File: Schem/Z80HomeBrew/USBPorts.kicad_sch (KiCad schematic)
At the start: 26 parts, among them J4 USB_A, J5 USB_A, U15 MAX3421EETJ_T, U16 FE1.1S-BSOP28BCN, U17 4050, Y2 ABL-12.000MHZ-B2, Y3 ABL-12.000MHZ-B2

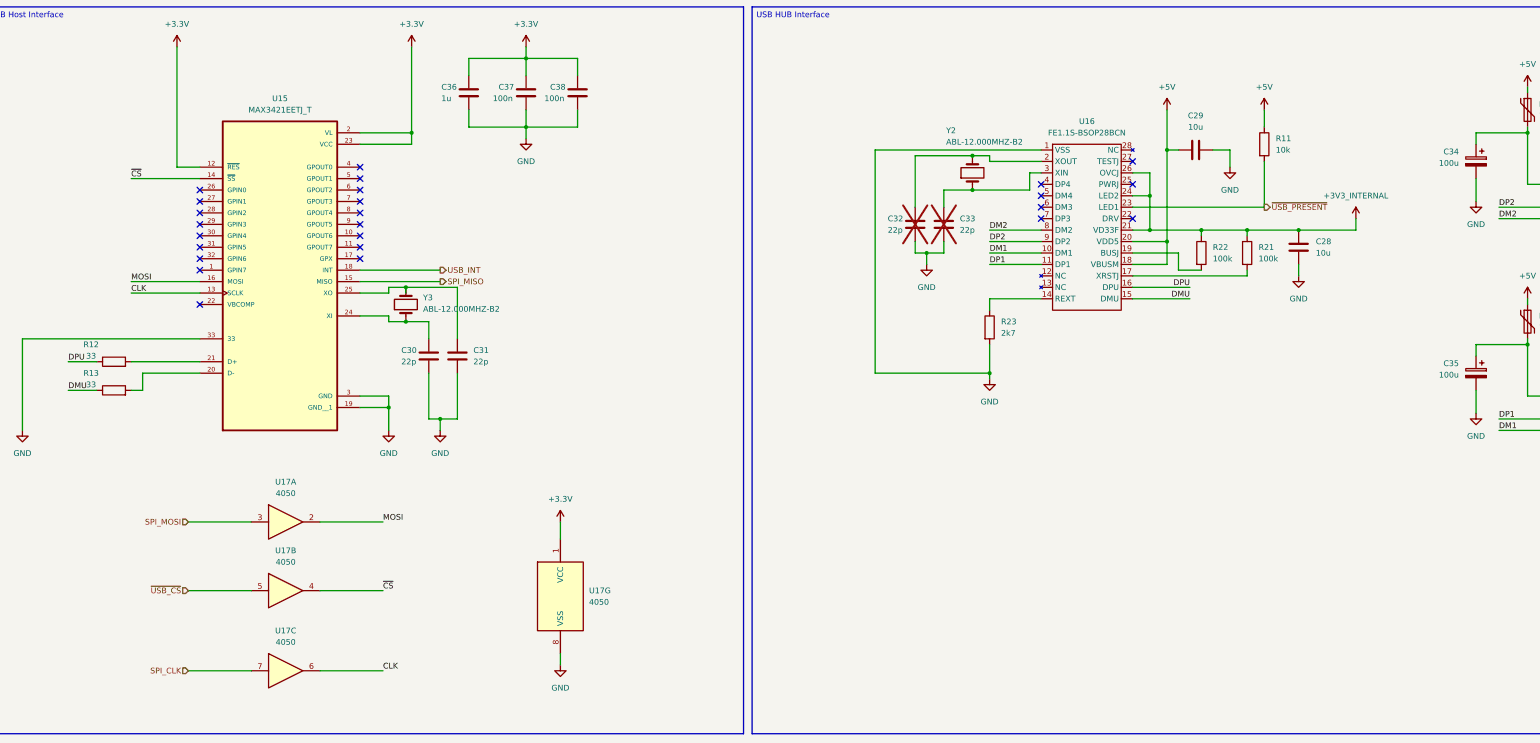
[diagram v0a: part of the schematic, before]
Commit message: Video block added. fixed some issues with parts...
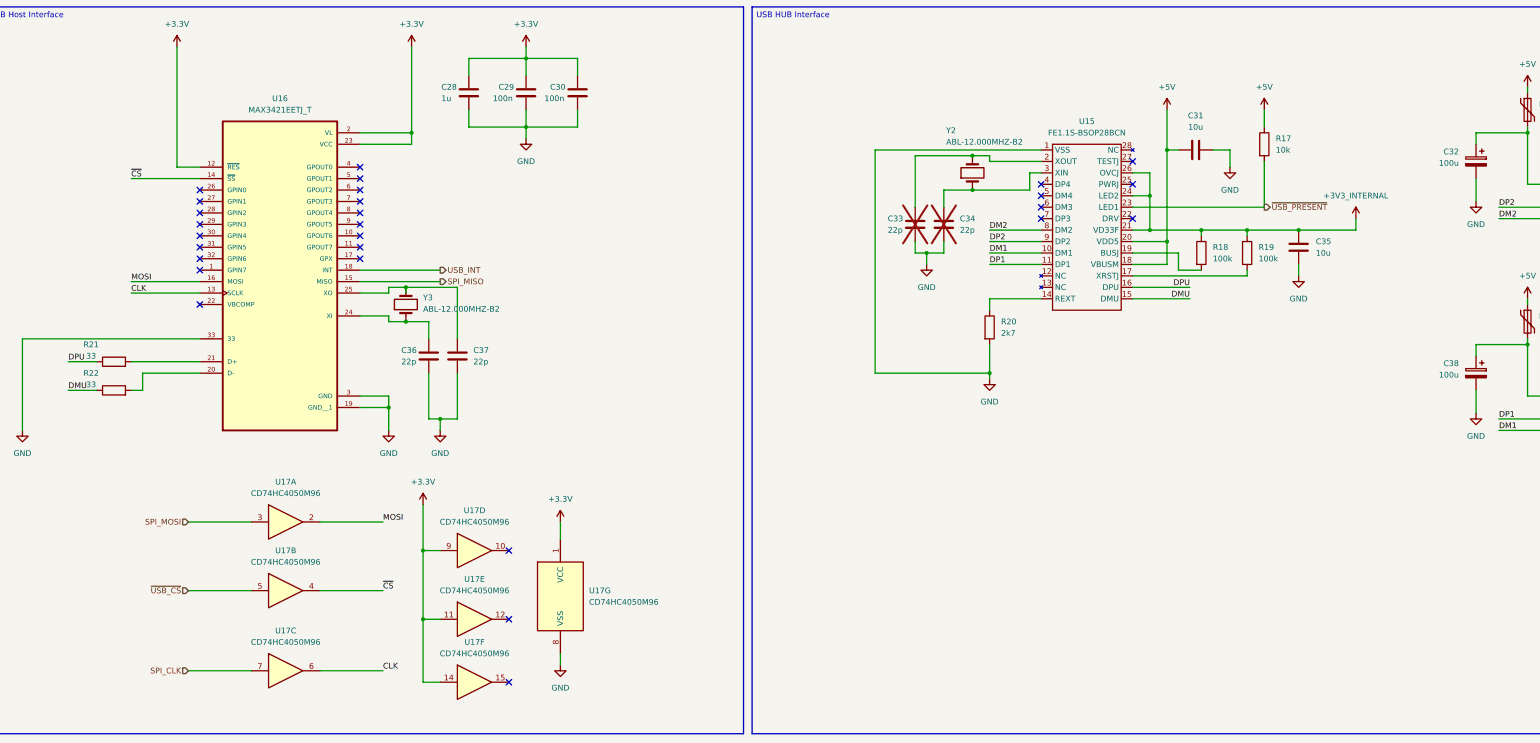
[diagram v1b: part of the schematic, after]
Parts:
- added unit 5 of U17
- added unit 4 of U17
- added unit 6 of U17
- C32: renamed from C34; footprint (none) -> Capacitor_SMD:C_0603_1608Metric
- C38: renamed from C35; footprint (none) -> Capacitor_SMD:C_0603_1608Metric
- U17: value 4050 -> CD74HC4050M96; footprint (none) -> Footprints:SOIC127P600X175-16N
- renumbered C36 to C28, C37 to C29, C38 to C30, C29 to C31, C32 to C33, C33 to C34, C28 to C35, C30 to C36, C31 to C37, R11 to R17, R22 to R18, R21 to R19, R23 to R20, R12 to R21, R13 to R22, U16 to U15, U15 to U16
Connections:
- net +3.3V: now also U17.11, U17.14, U17.9
- no-connect marks 25 -> 28

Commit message: Completed schematics
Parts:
- added R37: 0, NetTie:NetTie-2_SMD_Pad0.5mm, symbol Device:R
- J4, J5: value USB_A -> 0480370001; footprint (none) -> Footprints:CONN_480370001_MOL
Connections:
- net +3V3_INTERNAL: no longer U15.24 (LED2)
- net GND: now also R37.1; no longer U16.33
- new net: R37.2, U16.33
- no-connect marks 28 -> 29
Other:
- moved on the sheet: Y3

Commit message: Finally found a name "Zephyr-80" for the brew and committing the first pbc
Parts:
- added J14, J15: Conn_01x04, Connector_PinSocket_2.54mm:PinSocket_1x04_P2.54mm_Vertical, symbol Connector_Generic:Conn_01x04
- R37: now not fitted
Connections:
- net +3.3V: no longer U17.11, U17.14, U17.9
- net DM1: now also J15.2 (Pin_2)
- net DM2: now also J14.2 (Pin_2)
- net DP1: now also J15.4 (Pin_4)
- net DP2: now also J14.4 (Pin_4)
- net GND: now also U17.11, U17.14, U17.9, J14.3 (Pin_3), J15.3 (Pin_3)
- net at C36.2, U16.24 (XI): now also Y3.2; no longer Y3.1
- net at C37.2, U16.25 (XO): now also Y3.1; no longer Y3.2
- net VBUS_PIN2: now reaches C32.1, F2.2, J4.1 (VBUS)
- net VBUS_PIN2: now also J14.1 (Pin_1)
- net at C34.2, U15.3 (XIN): now also Y2.2; no longer Y2.1
- net at C33.2, U15.2 (XOUT): now also Y2.1; no longer Y2.2
- net VBUS_PIN1: now reaches C38.1, F3.2, J5.1 (VBUS)
- net VBUS_PIN1: now also J15.1 (Pin_1)
- net DMU renamed D-
- net DPU renamed D+
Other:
- note added: "Alternative header for USB Port"

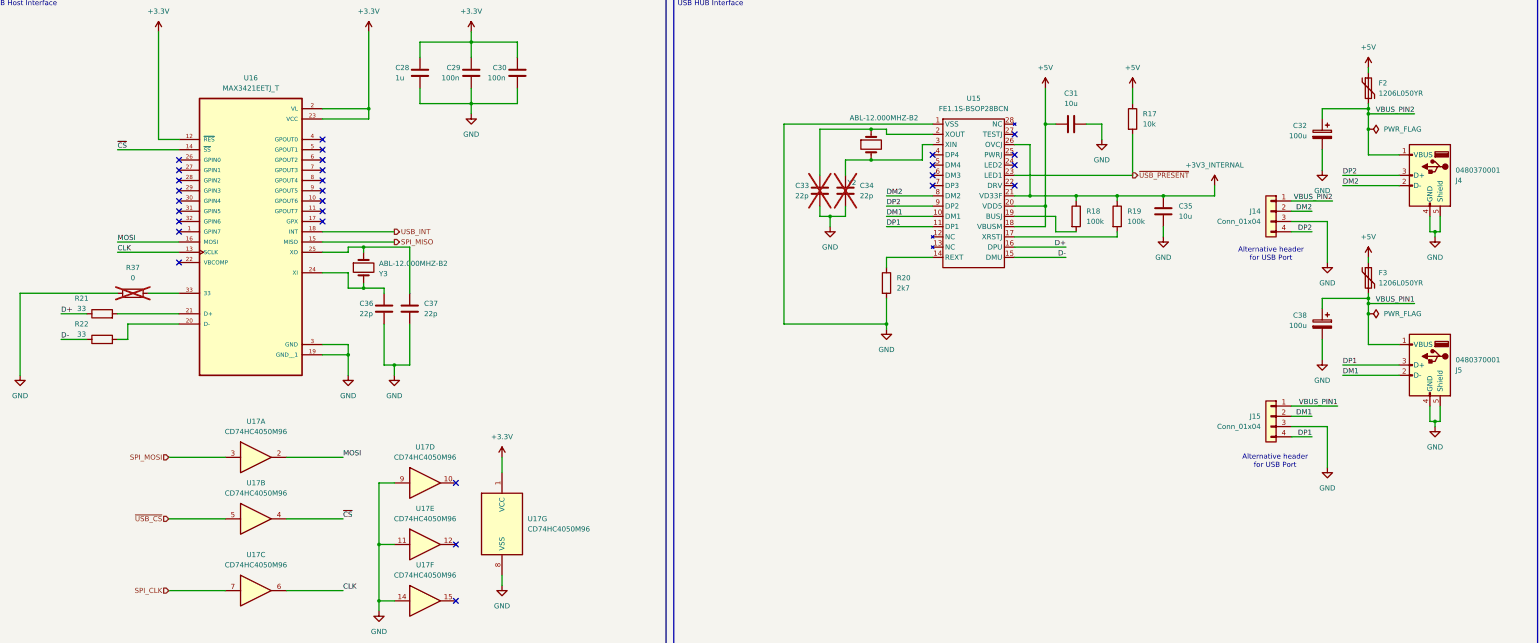
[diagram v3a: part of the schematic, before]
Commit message: Added pBITzBackplane and MezzanineConnector
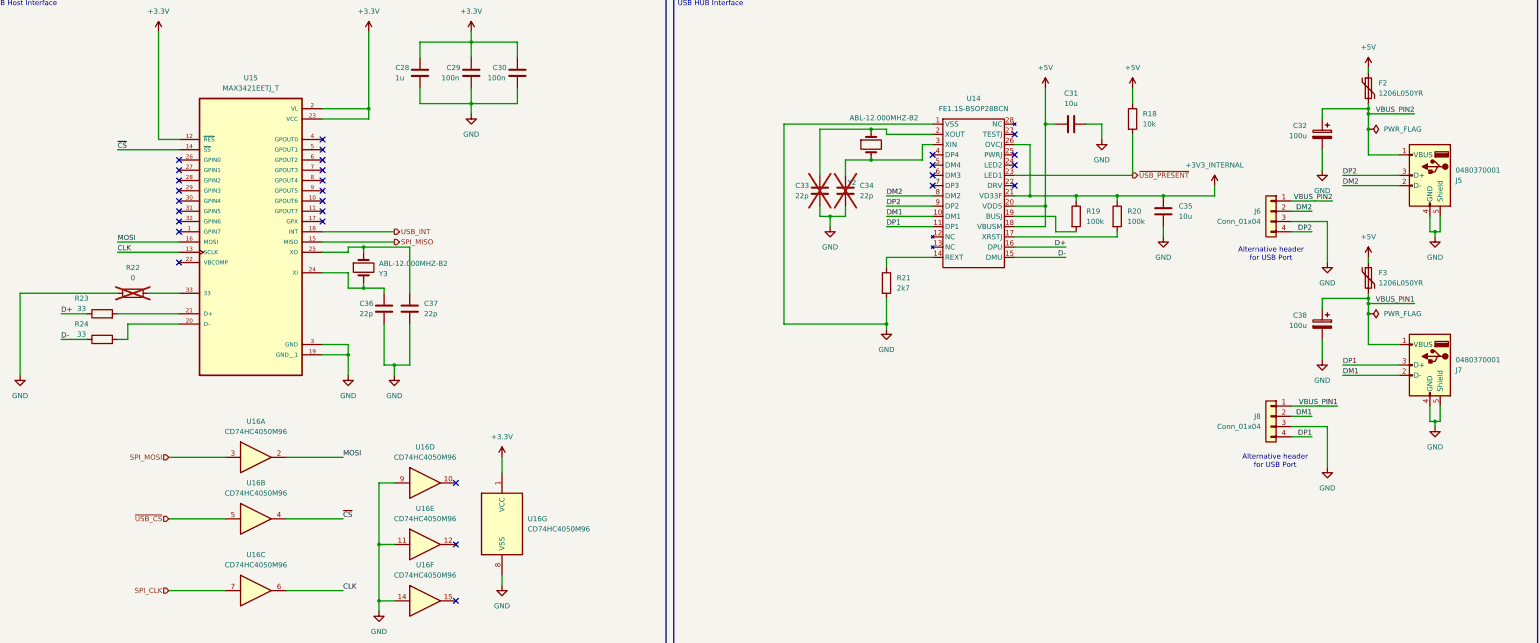
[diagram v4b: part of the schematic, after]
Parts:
- C28: MANUFACTURER_PART_NUMBER (none) -> C0603C105K4RACTU
- C29, C30: MANUFACTURER_PART_NUMBER (none) -> C0603C104K5RACTU
- C31, C35: MANUFACTURER_PART_NUMBER (none) -> CL10X106MO8NRNC
- C32, C38: footprint Capacitor_SMD:C_0603_1608Metric -> Capacitor_THT:CP_Radial_D5.0mm_P2.50mm; MANUFACTURER_PART_NUMBER (none) -> ECA-1CHG101I
- C36, C37: MANUFACTURER_PART_NUMBER (none) -> KGM15ACG1C220KT
- F2, F3: MANUFACTURER_PART_NUMBER (none) -> 1206L050YR
- J5: renamed from J4; MANUFACTURER_PART_NUMBER (none) -> MSD-1-A
- J6: renamed from J14; MANUFACTURER_PART_NUMBER (none) -> 732-5301-ND
- J7: renamed from J5; MANUFACTURER_PART_NUMBER (none) -> MSD-1-A
- J8: renamed from J15; MANUFACTURER_PART_NUMBER (none) -> 732-5301-ND
- R18: renamed from R17; MANUFACTURER_PART_NUMBER (none) -> RC0603FR-0710KL
- R19: renamed from R18; MANUFACTURER_PART_NUMBER (none) -> RMCF0603FT100K
- R20: renamed from R19; MANUFACTURER_PART_NUMBER (none) -> RMCF0603FT100K
- R21: renamed from R20; MANUFACTURER_PART_NUMBER (none) -> RC0603JR-072K7L
- R23: renamed from R21; MANUFACTURER_PART_NUMBER (none) -> RC0603FR-0733RL
- R24: renamed from R22; MANUFACTURER_PART_NUMBER (none) -> RC0603FR-0733RL
- U14: renamed from U15; MANUFACTURER_PART_NUMBER (none) -> FE1.1S-BSOP28BCN
- U15: renamed from U16; MANUFACTURER_PART_NUMBER (none) -> MAX3421EETJ+T
- U16: renamed from U17; MANUFACTURER_PART_NUMBER (none) -> CD74HC4050M96
- Y2, Y3: MANUFACTURER_PART_NUMBER (none) -> ABL-12.000MHZ-B2
- renumbered R37 to R22
